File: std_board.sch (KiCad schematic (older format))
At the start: 190 parts, among them IC1 ESP32, IC2 ACS712, IC3 L78L05, IC4 AMS1117-V, J1 Jumper, J10 J_DHT11, J11 Jumper, J12 Jumper, J14 Jumper, J15 Jumper, J16 J_PRess, J17 Jumper, J18 Jumper, J19 Jumper, J2 Jumper, J20 Jumper, J21 Jumper, J22 Jumper, J23 Jumper, J24 Jumper, J25 Jumper, J26 Jumper, J3 Jumper, J31 Jumper, J32 Jumper, J33 Jumper, J34 Jumper, J35 Jumper, J36 Jumper, J37 Jumper, J38 Jumper, J39 Jumper, J4 Jumper, J40 Jumper, J41 Jumper, J42 Jumper, J43 Jumper, J44 Jumper, J45 Jumper, J5 Jumper, J9 Jumper, T1 TRIAC_Micro, T2 TRIAC_Micro, T3 TRIAC_Micro, T4 NPN_MMBT222A, T5 NPN_MMBT222A, T6 NPN_MMBT222A, T7 NPN_MMBT222A, T8 PNP_2N3906, T9 NPN_MMBT222A, U1 LNK306

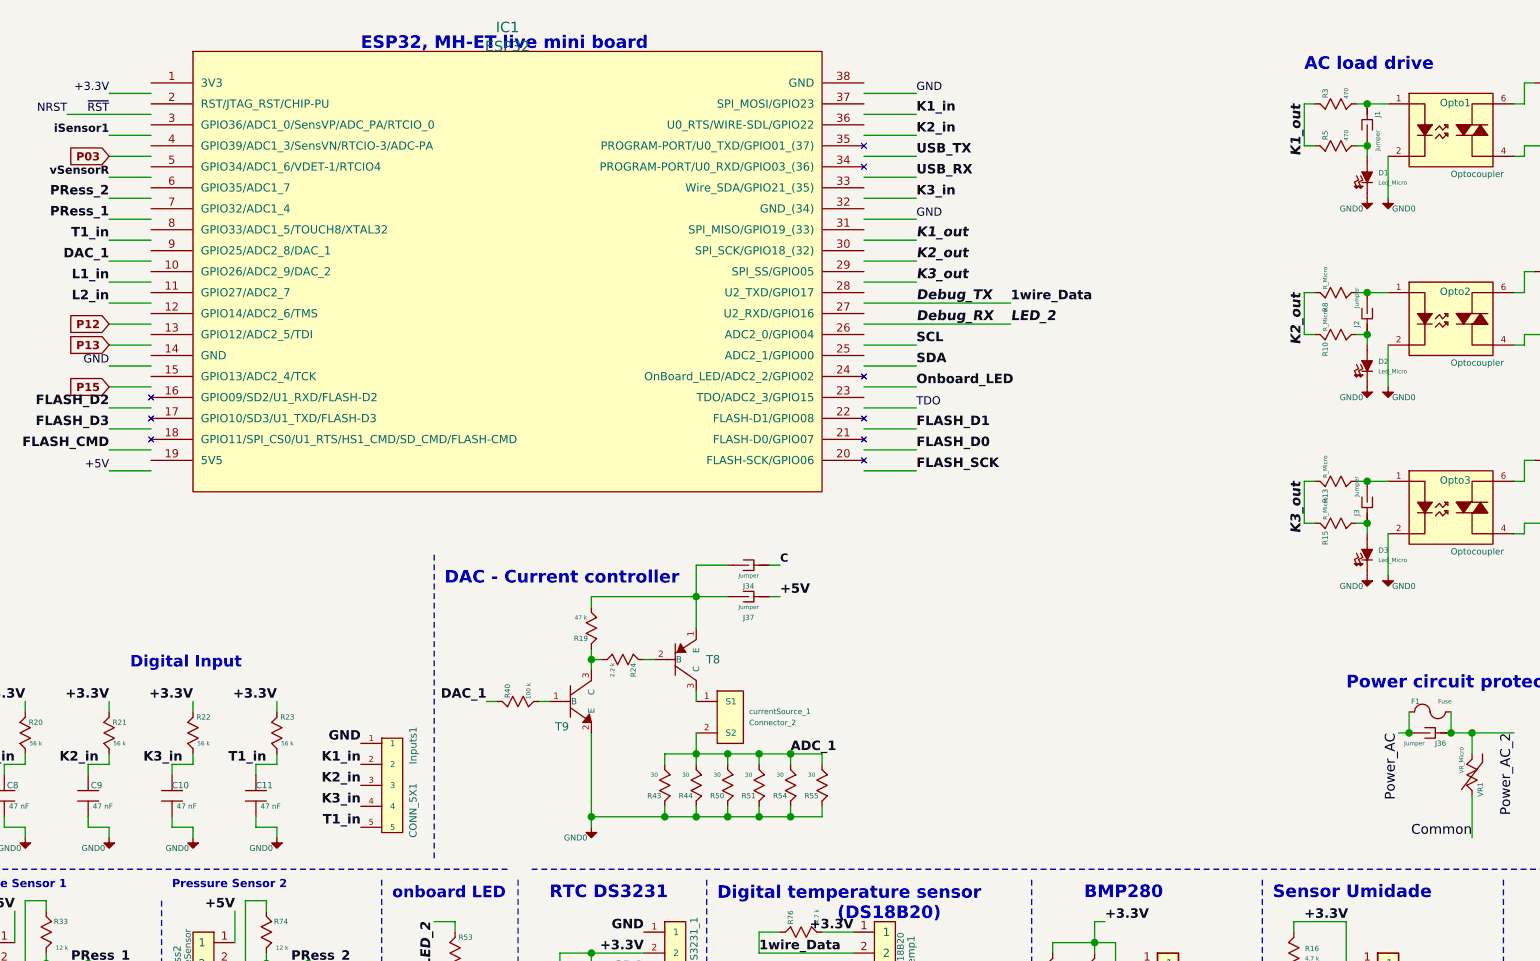
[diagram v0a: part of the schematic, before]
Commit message: added new triac circuit upgrade to soft starter
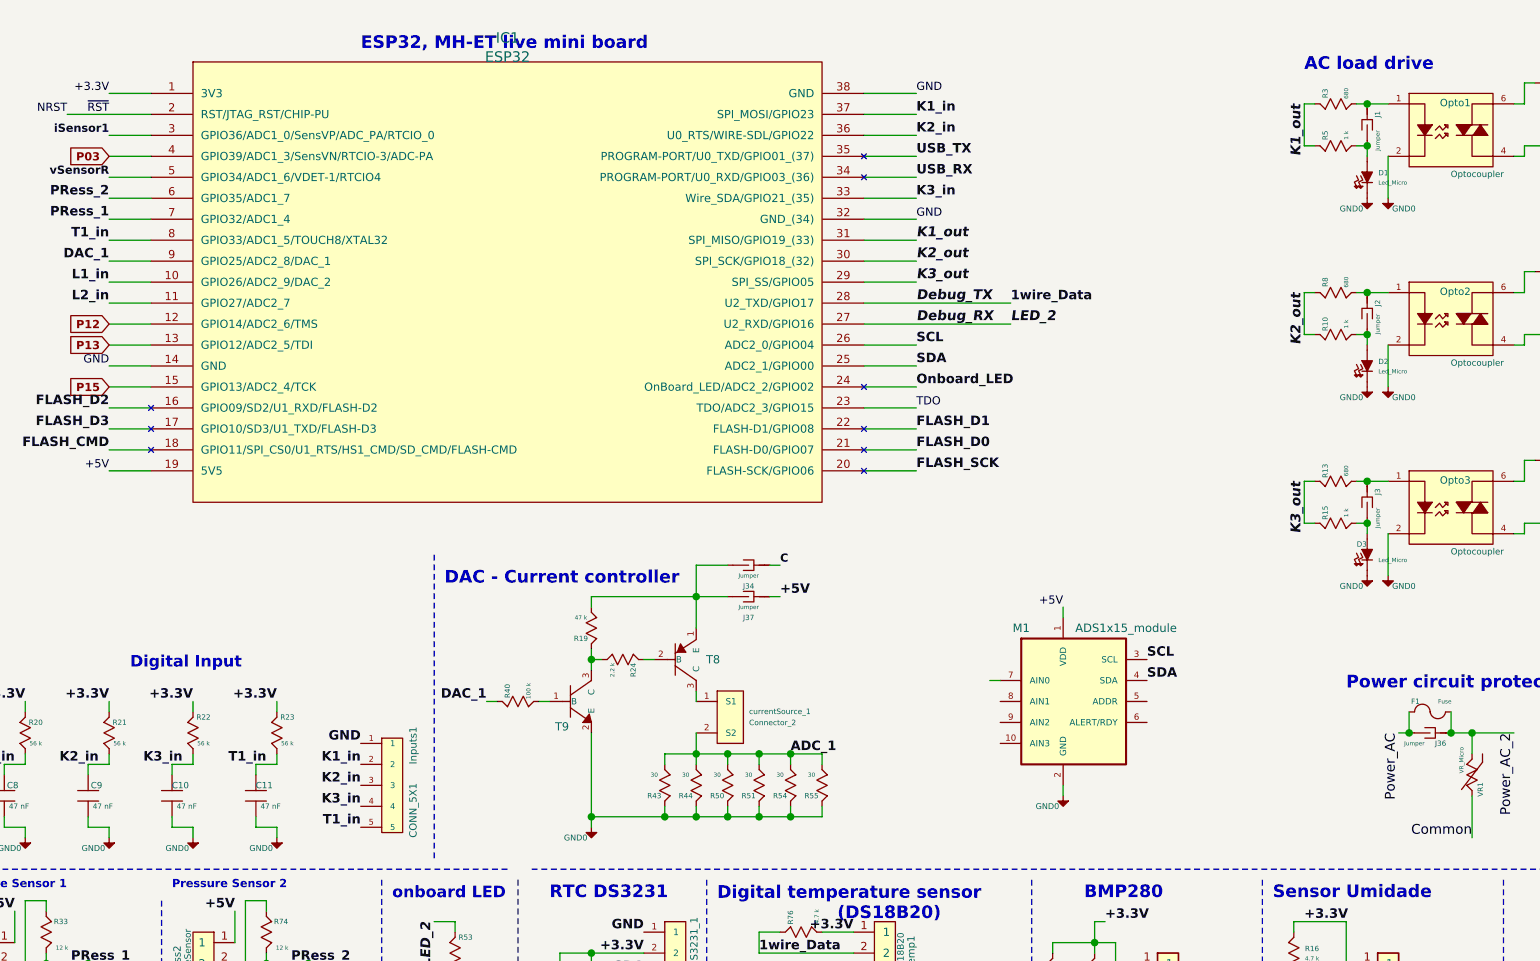
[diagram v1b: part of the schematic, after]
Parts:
- added M1: ADS1x15_module, Connector_PinHeader_2.54mm:PinHeader_1x10_P2.54mm_Vertical, symbol thmalmeida:ADS1x15_module
- Opto1: Manufacturer MMMM -> (none)
- Opto2, Opto3: Manufacturer MMMM -> (none); manf# (none) -> MOC3021M
- R10, R15: value R_Micro -> 1 k
- R13, R8: value R_Micro -> 680
- R3: value 470 -> 680
- R5: value 470 -> 1 k
- T1: Manufacturer MMMM -> BT136
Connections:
- wire segments 580 -> 583
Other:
- moved on the sheet: IC1
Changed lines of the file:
@@
 F 3 "" H 9750 1150 60  0000 C CNN
 F 4 "xxxx" H 9650 1400 60  0001 C CNN "Part Number"
-F 5 "MMMM" H 9650 1500 60  0001 C CNN "Manufacturer"
-F 6 "yes" H 9650 1600 60  0001 C CNN "Placed Onboard?"
+F 5 "yes" H 9650 1600 60  0001 C CNN "Placed Onboard?"
 	1    9650 1000
 	1    0    0    -1
@@
 P 9100 850
 F 0 "R3" H 9150 900 25  0000 C CNN
-F 1 "470" H 9150 800 20  0000 C CNN
+F 1 "680" H 9150 800 20  0000 C CNN
 F 2 "Resistor_SMD:R_0805_2012Metric" H 8930 800 60  0001 C CNN
 F 3 "" H 9030 900 60  0000 C CNN
@@
 F 3 "" H 10650 1100 60  0000 C CNN
 F 4 "xxxx" H 10750 1200 60  0001 C CNN "Part Number"
-F 5 "MMMM" H 10850 1300 60  0001 C CNN "Manufacturer"
+F 5 "BT136" H 10850 1300 60  0001 C CNN "Manufacturer"
 F 6 "yes" H 10950 1400 60  0001 C CNN "Placed Onboard?"
 	1    10600 950
@@
 F 3 "" H 9750 2050 60  0000 C CNN
 F 4 "xxxx" H 9650 2300 60  0001 C CNN "Part Number"
-F 5 "MMMM" H 9650 2400 60  0001 C CNN "Manufacturer"
-F 6 "yes" H 9650 2500 60  0001 C CNN "Placed Onboard?"
+F 5 "yes" H 9650 2500 60  0001 C CNN "Placed Onboard?"
+F 6 "MOC3021M" H 9650 1900 50  0001 C CNN "manf#"
 	1    9650 1900
 	1    0    0    -1
@@
 U 1 1 5D53DD86
 P 9100 1750
-F 0 "R8" H 9030 1800 25  0000 C CNN
-F 1 "R_Micro" H 9170 1800 20  0000 C CNN
+F 0 "R8" H 9150 1700 25  0000 C CNN
+F 1 "680" H 9150 1800 20  0000 C CNN
 F 2 "Resistor_SMD:R_0805_2012Metric" H 8930 1700 60  0001 C CNN
 F 3 "" H 9030 1800 60  0000 C CNN
@@
 F 9 "5" H 100 200 50  0001 C CNN "Tolerance [%]"
 	1    9100 1750
-	0    -1   -1   0
+	0    1    -1   0
 $EndComp
 $Comp
@@
 U 1 1 5D53DDB8
 P 9250 1850
-F 0 "J2" H 9200 1900 25  0000 C CNN
-F 1 "Jumper" H 9325 1900 20  0000 C CNN
+F 0 "J2" H 9200 1800 25  0000 C CNN
+F 1 "Jumper" H 9300 1800 20  0000 C CNN
 F 2 "thmalmeida:J_0603" H 9275 1850 60  0001 C CNN
 F 3 "" H 9275 1850 60  0000 C CNN
 	1    9250 1850
-	0    -1   -1   0
+	0    -1   1    0
 $EndComp
 $Comp
@@
 U 1 1 5D53DDC7
 P 9100 1950
-F 0 "R10" H 9030 2000 25  0000 C CNN
-F 1 "R_Micro" H 9170 2000 20  0000 C CNN
+F 0 "R10" H 9150 2000 25  0000 C CNN
+F 1 "1 k" H 9150 1900 20  0000 C CNN
 F 2 "Resistor_SMD:R_0805_2012Metric" H 8930 1900 60  0001 C CNN
 F 3 "" H 9030 2000 60  0000 C CNN
@@
 F 3 "" H 9750 2950 60  0000 C CNN
 F 4 "xxxx" H 9650 3200 60  0001 C CNN "Part Number"
-F 5 "MMMM" H 9650 3300 60  0001 C CNN "Manufacturer"
-F 6 "yes" H 9650 3400 60  0001 C CNN "Placed Onboard?"
+F 5 "yes" H 9650 3400 60  0001 C CNN "Placed Onboard?"
+F 6 "MOC3021M" H 9650 2800 50  0001 C CNN "manf#"
 	1    9650 2800
 	1    0    0    -1
@@
 U 1 1 5D5FE185
 P 9100 2650
-F 0 "R13" H 9030 2700 25  0000 C CNN
-F 1 "R_Micro" H 9170 2700 20  0000 C CNN
+F 0 "R13" H 9150 2700 25  0000 C CNN
+F 1 "680" H 9150 2600 20  0000 C CNN
 F 2 "Resistor_SMD:R_0805_2012Metric" H 8930 2600 60  0001 C CNN
 F 3 "" H 9030 2700 60  0000 C CNN
@@
 F 3 "" H 9275 2750 60  0000 C CNN
 	1    9250 2750
-	0    -1   -1   0
+	0    1    1    0
 $EndComp
 $Comp
@@
 U 1 1 5D5FE1C6
 P 9100 2850
-F 0 "R15" H 9030 2900 25  0000 C CNN
-F 1 "R_Micro" H 9170 2900 20  0000 C CNN
+F 0 "R15" H 9150 2900 25  0000 C CNN
+F 1 "1 k" H 9150 2800 20  0000 C CNN
 F 2 "Resistor_SMD:R_0805_2012Metric" H 8930 2800 60  0001 C CNN
 F 3 "" H 9030 2900 60  0000 C CNN
@@
 U 1 1 63A66F3B
 P 9250 3000
-F 0 "D3" V 9229 3053 25  0000 L CNN
+F 0 "D3" V 9200 2950 25  0000 L CNN
 F 1 "Led_Micro" V 9276 3053 20  0000 L CNN
 F 2 "LED_SMD:LED_0805_2012Metric" H 9240 2900 60  0001 C CNN
@@
 P 9100 1050
 F 0 "R5" H 9150 1100 25  0000 C CNN
-F 1 "470" H 9150 1000 20  0000 C CNN
+F 1 "1 k" H 9150 1000 20  0000 C CNN
 F 2 "Resistor_SMD:R_0805_2012Metric" H 8930 1000 60  0001 C CNN
 F 3 "" H 9030 1100 60  0000 C CNN
@@
 L thmalmeida:ESP32 IC1
 U 1 1 6140C67D
-P 5150 1750
-F 0 "IC1" H 5150 3015 50  0000 C CNN
-F 1 "ESP32" H 5150 2924 50  0000 C CNN
-F 2 "thmalmeida:ESP32_DEVKIT" H 5200 2950 60  0001 C CNN
-F 3 "https://www.espressif.com/sites/default/files/documentation/esp32_datasheet_en.pdf" H 4900 1000 60  0001 C CNN
-F 4 "Espressif" H 5250 3200 60  0001 C CNN "Manufacturer"
-F 5 "ESP-WROOM-32" H 5250 3100 60  0001 C CNN "Partnumber"
-F 6 "https://www.espressif.com/sites/default/files/documentation/esp32_technical_reference_manual_en.pdf" H 5150 1750 50  0001 C CNN "Technical Manual"
-	1    5150 1750
+P 5150 1800
+F 0 "IC1" H 5150 3065 50  0000 C CNN
+F 1 "ESP32" H 5150 2974 50  0000 C CNN
+F 2 "thmalmeida:ESP32_DEVKIT" H 5200 3000 60  0001 C CNN
+F 3 "https://www.espressif.com/sites/default/files/documentation/esp32_datasheet_en.pdf" H 4900 1050 60  0001 C CNN
+F 4 "Espressif" H 5250 3250 60  0001 C CNN "Manufacturer"
+F 5 "ESP-WROOM-32" H 5250 3150 60  0001 C CNN "Partnumber"
+F 6 "https://www.espressif.com/sites/default/files/documentation/esp32_technical_reference_manual_en.pdf" H 5150 1800 50  0001 C CNN "Technical Manual"
+	1    5150 1800
 	1    0    0    -1
 $EndComp
@@
 Text GLabel 3250 1100 0    39   Input ~ 8
 P03
+Text Label 7800 3250 2    39   ~ 0
++5V
+Wire Wire Line
+	7800 3300 7800 3250
+Wire Wire Line
+	7800 4100 7800 4150
+$Comp
+L std_board-rescue:GND0-thmalmeida #PWR026
+U 1 1 61A8D185
+P 7800 4150
+F 0 "#PWR026" H 7800 3900 50  0001 C CNN
+F 1 "GND0" H 7875 4100 28  0000 C CNN
+F 2 "" H 7800 4150 60  0000 C CNN
+F 3 "" H 7800 4150 60  0000 C CNN
+	1    7800 4150
+	-1   0    0    -1
+$EndComp
+Text Label 8200 3600 0    45   ~ 9
+SDA
+Text Label 8200 3500 0    45   ~ 9
+SCL
+Wire Wire Line
+	7500 3600 7450 3600
+$Comp
+L thmalmeida:ADS1x15_module M1
+U 1 1 616C1D9A
+P 7800 3700
+F 0 "M1" H 7600 4050 40  0000 C CNN
+F 1 "ADS1x15_module" H 8100 4050 40  0000 C CNN
+F 2 "Connector_PinHeader_2.54mm:PinHeader_1x10_P2.54mm_Vertical" H 8300 4350 40  0001 C CNN
+F 3 "" H 8300 4350 40  0001 C CNN
+	1    7800 3700
+	1    0    0    -1
+$EndComp
 $EndSCHEMATC
